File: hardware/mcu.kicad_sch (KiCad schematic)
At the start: 34 parts, among them J2 EXT, J3 SW, J4 USB_B_Mini, SW1 BTN_ACT, SW2 BTN_DEACT, U1 STM32F103C8T6, Y1 32KHz, Y2 8MHz

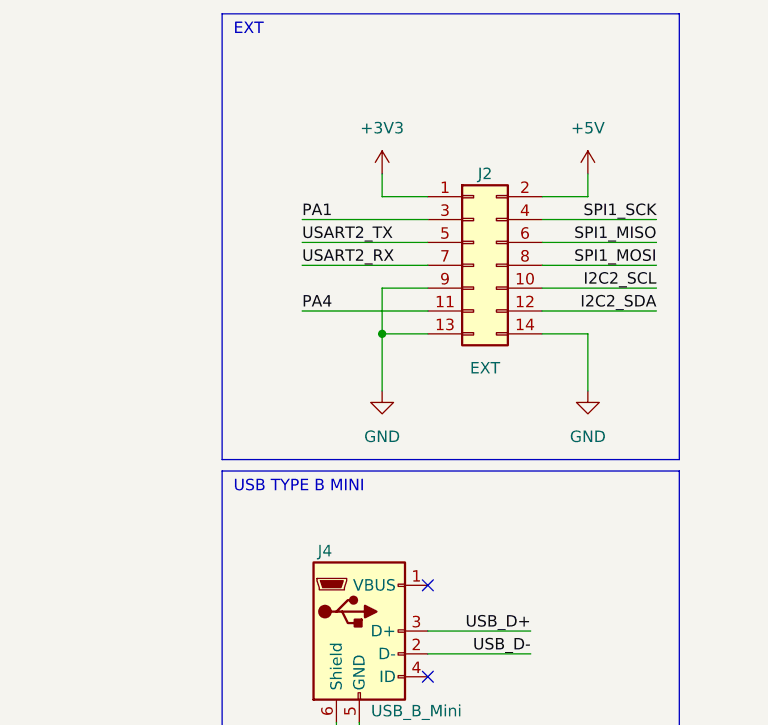
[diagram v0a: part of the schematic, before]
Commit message: * 3V8 Power design fixed * Footprints assigned * Bom exported * PCB filter module placed
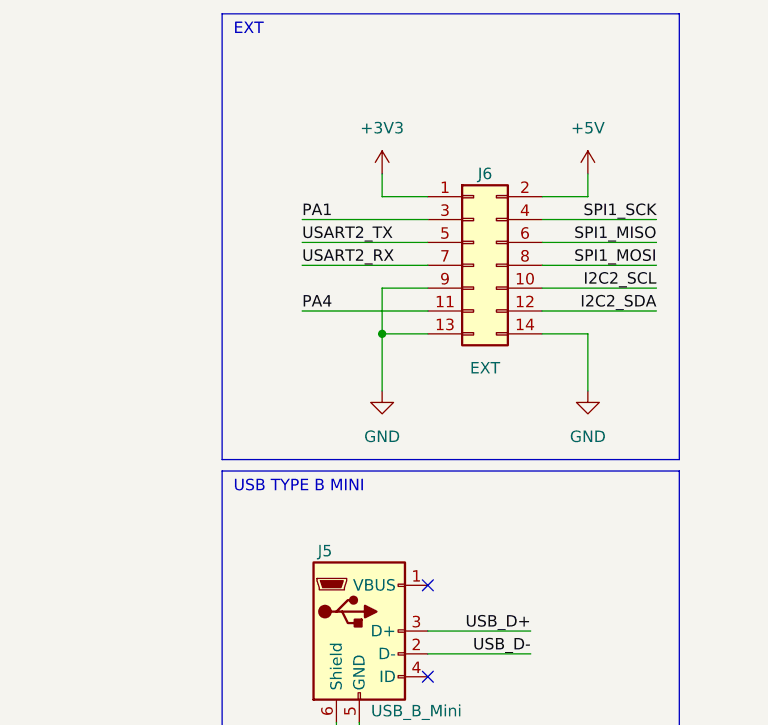
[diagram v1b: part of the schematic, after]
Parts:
- J5: renamed from J4; footprint (none) -> Connector_USB:USB_Mini-B_Wuerth_65100516121_Horizontal; Digikey (none) -> 732-2109-2-ND
- J6: renamed from J2; footprint (none) -> 2023Staj:CONN14_1421621_WRE; Digikey (none) -> 732-5397-ND
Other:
- company: (none) -> Hidro Elektronik
- title: (none) -> 2023 Staj Projesi

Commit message: PCB design completed
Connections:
- net I2C2_SCL: now also J6.12 (Pin_12); no longer J6.10 (Pin_10)
- net I2C2_SDA: now also J6.10 (Pin_10); no longer J6.12 (Pin_12)
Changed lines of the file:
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@@
     (effects (font (size 1.27 1.27)) (justify left bottom))
   )
-  (label "I2C2_SDA" (at 276.86 48.26 180) (fields_autoplaced)
+  (label "I2C2_SDA" (at 276.86 45.72 180) (fields_autoplaced)
     (effects (font (size 1.27 1.27)) (justify right bottom))
   )
@@
     (effects (font (size 1.27 1.27)) (justify right bottom))
   )
-  (label "I2C2_SCL" (at 276.86 45.72 180) (fields_autoplaced)
+  (label "I2C2_SCL" (at 276.86 48.26 180) (fields_autoplaced)
     (effects (font (size 1.27 1.27)) (justify right bottom))
   )
